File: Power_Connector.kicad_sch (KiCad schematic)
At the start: 4 parts, among them J2 AMASS XT60 Male, J3 AMASS XT60 Male, J7 AMASS XT60 Female

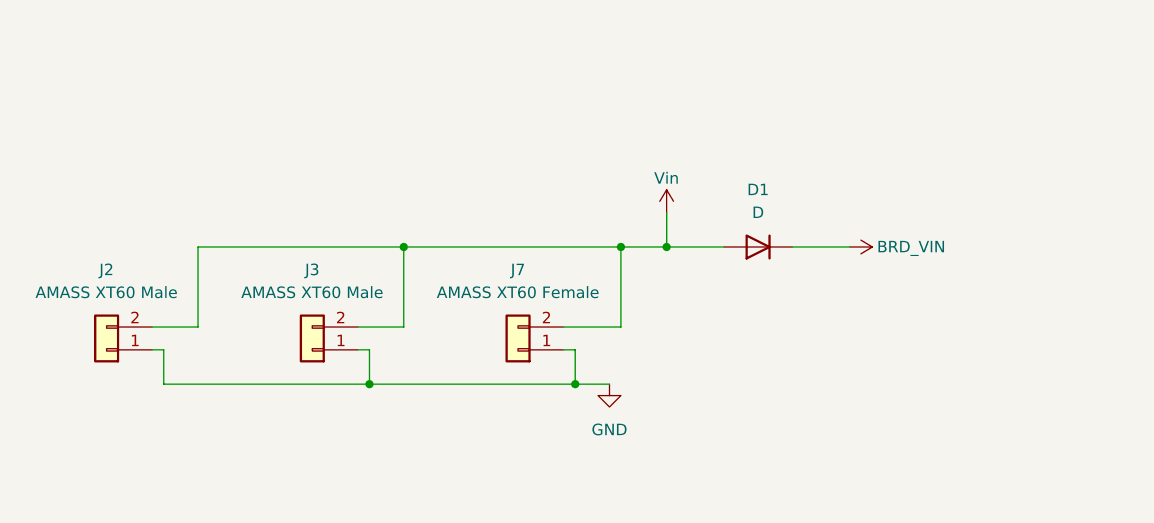
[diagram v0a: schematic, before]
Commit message: finished schematic (without some part numbers)
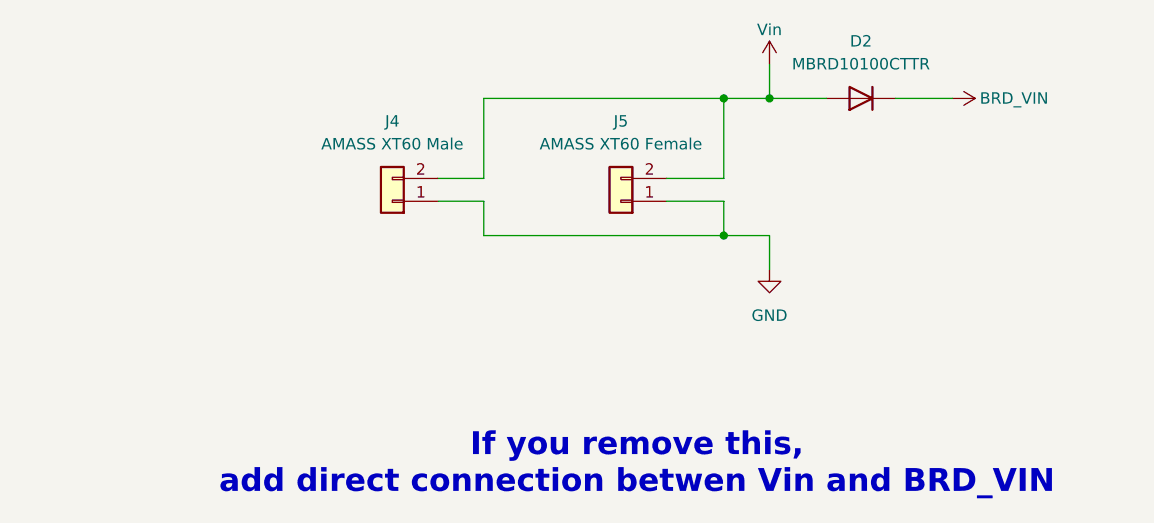
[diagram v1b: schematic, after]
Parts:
- removed D1: D, symbol Device:D
- removed J3: AMASS XT60 Male, XT60:AMASS_XT60PW-M_1x02_P7.20mm_Horizontal, symbol Connector_Generic:Conn_01x02
- added D2: MBRD10100CTTR, symbol Device:D
- renumbered J2 to J4, J7 to J5
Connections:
- net BRD_VIN: now also D2.1 (K)
- net Vin: now also D2.2 (A)
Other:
- note added: "If you remove this, add direct connection betwen Vin and BRD_VIN"
- moved on the sheet: J4, J5

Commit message: initial component placement
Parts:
- D2: footprint (none) -> Package_TO_SOT_SMD:TO-252-2
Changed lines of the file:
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@@
 			)
 		)
-		(property "Footprint" ""
+		(property "Footprint" "Package_TO_SOT_SMD:TO-252-2"
 			(at 167.64 86.36 0)
 			(effects

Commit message: revision
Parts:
- removed D2: MBRD10100CTTR, Package_TO_SOT_SMD:TO-252-2, symbol Device:D
- added D4: MBRD10100CTTR, SMC_MBRD10100CTTR:TO-252-3_L6.5-W5.8-P4.58-TL, symbol SMC_MBRD10100CTTR:MBRD10100CTTR
- J4, J5: now left out of the parts list
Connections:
- net BRD_VIN: now also D4.2 (K)
- net Vin: now also D4.1, D4.3
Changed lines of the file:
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@@
+	)
+	(junction
+		(at 161.29 86.36)
+		(diameter 0)
+		(color 0 0 0 0)
 	)
 	(junction
@@
 	(wire
 		(pts
+			(xy 161.29 86.36) (xy 163.83 86.36)
+		)
+		(stroke
+			(width 0)
+			(type default)
+		)
+	)
+	(wire
+		(pts
 			(xy 152.4 86.36) (xy 157.48 86.36)
 		)
@@
 	(wire
 		(pts
-			(xy 157.48 86.36) (xy 163.83 86.36)
+			(xy 157.48 86.36) (xy 161.29 86.36)
+		)
+		(stroke
+			(width 0)
+			(type default)
+		)
+	)
+	(wire
+		(pts
+			(xy 161.29 91.44) (xy 161.29 86.36)
+		)
+		(stroke
+			(width 0)
+			(type default)
+		)
+	)
+	(wire
+		(pts
+			(xy 163.83 91.44) (xy 161.29 91.44)
 		)
 		(stroke
@@
 	(wire
 		(pts
-			(xy 171.45 86.36) (xy 177.8 86.36)
+			(xy 179.07 88.9) (xy 185.42 88.9)
 		)
 		(stroke
@@
 		(unit 1)
 		(exclude_from_sim no)
-		(in_bom yes)
+		(in_bom no)
 		(on_board yes)
 		(dnp no)
@@
 	(symbol
 		(lib_id "power:VCC")
-		(at 177.8 86.36 270)
+		(at 185.42 88.9 270)
 		(unit 1)
 		(exclude_from_sim no)
@@
 		(on_board yes)
 		(dnp no)
-		(property "Reference" "#PWR041"
-			(at 173.99 86.36 0)
+		(property "Reference" "#PWR042"
+			(at 181.61 88.9 0)
 			(effects
 				(font
@@
 		)
 		(property "Value" "BRD_VIN"
-			(at 184.658 86.36 90)
+			(at 192.278 88.9 90)
 			(effects
 				(font
@@
 		)
 		(property "Footprint" ""
-			(at 177.8 86.36 0)
+			(at 185.42 88.9 0)
 			(effects
 				(font
@@
 		)
 		(property "Datasheet" ""
-			(at 177.8 86.36 0)
+			(at 185.42 88.9 0)
 			(effects
 				(font
@@
 		)
 		(property "Description" "Power symbol creates a global label with name \"VCC\""
-			(at 177.8 86.36 0)
+			(at 185.42 88.9 0)
 			(effects
 				(font
@@
 			(project "MMS2_hat_template_small"
 				(path "/6596548a-44e0-46d8-8624-fd71cf4a3e17/f11c3b61-ae6a-4858-9d37-bbf426f44fb0"
-					(reference "#PWR041")
+					(reference "#PWR042")
 					(unit 1)
 				)
@@
 		(unit 1)
 		(exclude_from_sim no)
-		(in_bom yes)
+		(in_bom no)
 		(on_board yes)
 		(dnp no)
@@
 		(on_board yes)
 		(dnp no)
-		(property "Reference" "#PWR039"
+		(property "Reference" "#PWR040"
 			(at 157.48 86.36 0)
 			(effects
@@
 			(project "MMS2_hat_template_small"
 				(path "/6596548a-44e0-46d8-8624-fd71cf4a3e17/f11c3b61-ae6a-4858-9d37-bbf426f44fb0"
-					(reference "#PWR039")
+					(reference "#PWR040")
 					(unit 1)
 				)
@@
 	)
 	(symbol
-		(lib_id "Device:D")
-		(at 167.64 86.36 180)
+		(lib_id "SMC_MBRD10100CTTR:MBRD10100CTTR")
+		(at 171.45 88.9 0)
 		(unit 1)
 		(exclude_from_sim no)
@@
 		(dnp no)
 		(fields_autoplaced yes)
-		(property "Reference" "D2"
-			(at 167.64 80.01 0)
-			(effects
-				(font
-					(size 1.27 1.27)
-				)
+		(property "Reference" "D4"
+			(at 172.7201 93.98 90)
+			(effects
+				(font
+					(size 1.27 1.27)
+				)
+				(justify right)
 			)
 		)
 		(property "Value" "MBRD10100CTTR"
-			(at 167.64 82.55 0)
-			(effects
-				(font
-					(size 1.27 1.27)
-				)
-			)
-		)
-		(property "Footprint" "Package_TO_SOT_SMD:TO-252-2"
-			(at 167.64 86.36 0)
-			(effects
-				(font
-					(size 1.27 1.27)
-				)
-				(hide yes)
-			)
-		)
-		(property "Datasheet" "~"
-			(at 167.64 86.36 0)
-			(effects
-				(font
-					(size 1.27 1.27)
-				)
-				(hide yes)
-			)
-		)
-		(property "Description" "Diode"
-			(at 167.64 86.36 0)
-			(effects
-				(font
-					(size 1.27 1.27)
-				)
-				(hide yes)
-			)
-		)
-		(property "Sim.Device" "D"
-			(at 167.64 86.36 0)
-			(effects
-				(font
-					(size 1.27 1.27)
-				)
-				(hide yes)
-			)
-		)
-		(property "Sim.Pins" "1=K 2=A"
-			(at 167.64 86.36 0)
-			(effects
-				(font
-					(size 1.27 1.27)
-				)
-				(hide yes)
-			)
-		)
-		(property "LCSC" "C135494"
-			(at 167.64 86.36 90)
-			(effects
-				(font
-					(size 1.27 1.27)
-				)
-				(hide yes)
-			)
+			(at 170.1801 93.98 90)
+			(effects
+				(font
+					(size 1.27 1.27)
+				)
+				(justify right)
+			)
+		)
+		(property "Footprint" "SMC_MBRD10100CTTR:TO-252-3_L6.5-W5.8-P4.58-TL"
+			(at 171.45 99.06 0)
+			(effects
+				(font
+					(size 1.27 1.27)
+				)
+				(hide yes)
+			)
+		)
+		(property "Datasheet" "https://lcsc.com/product-detail/Schottky-Barrier-Diodes-SBD_MCC_MBRD10100CTTR_MBRD10100CTTR_C135494.html"
+			(at 171.45 101.6 0)
+			(effects
+				(font
+					(size 1.27 1.27)
+				)
+				(hide yes)
+			)
+		)
+		(property "Description" ""
+			(at 171.45 88.9 0)
+			(effects
+				(font
+					(size 1.27 1.27)
+				)
+				(hide yes)
+			)
+		)
+		(property "LCSC Part" "C135494"
+			(at 171.45 104.14 0)
+			(effects
+				(font
+					(size 1.27 1.27)
+				)
+				(hide yes)
+			)
+		)
+		(pin "1"
 		)
 		(pin "2"
 		)
-		(pin "1"
+		(pin "3"
 		)
 		(instances
 			(project "MMS3_hat_stepper_controler"
 				(path "/6596548a-44e0-46d8-8624-fd71cf4a3e17/f11c3b61-ae6a-4858-9d37-bbf426f44fb0"
-					(reference "D2")
+					(reference "D4")
 					(unit 1)
 				)
@@
 		(dnp no)
 		(fields_autoplaced yes)
-		(property "Reference" "#PWR040"
+		(property "Reference" "#PWR041"
 			(at 157.48 111.76 0)
 			(effects
@@
 			(project ""
 				(path "/6596548a-44e0-46d8-8624-fd71cf4a3e17/f11c3b61-ae6a-4858-9d37-bbf426f44fb0"
-					(reference "#PWR040")
+					(reference "#PWR041")
 					(unit 1)
 				)

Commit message: second component placement
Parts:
- renumbered D4 to D2
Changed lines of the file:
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@@
+			)
+		)
+		(property "Sim.Device" ""
+			(at 115.57 97.79 0)
+			(effects
+				(font
+					(size 1.27 1.27)
+				)
+				(hide yes)
 			)
 		)
@@
 		(on_board yes)
 		(dnp no)
-		(property "Reference" "#PWR042"
+		(property "Reference" "#PWR041"
 			(at 181.61 88.9 0)
 			(effects
@@
 			(project "MMS2_hat_template_small"
 				(path "/6596548a-44e0-46d8-8624-fd71cf4a3e17/f11c3b61-ae6a-4858-9d37-bbf426f44fb0"
-					(reference "#PWR042")
+					(reference "#PWR041")
 					(unit 1)
 				)
@@
 			)
 		)
+		(property "Sim.Device" ""
+			(at 140.97 97.79 0)
+			(effects
+				(font
+					(size 1.27 1.27)
+				)
+				(hide yes)
+			)
+		)
 		(pin "1"
 		)
@@
 		(on_board yes)
 		(dnp no)
-		(property "Reference" "#PWR040"
+		(property "Reference" "#PWR039"
 			(at 157.48 86.36 0)
 			(effects
@@
 			(project "MMS2_hat_template_small"
 				(path "/6596548a-44e0-46d8-8624-fd71cf4a3e17/f11c3b61-ae6a-4858-9d37-bbf426f44fb0"
-					(reference "#PWR040")
+					(reference "#PWR039")
 					(unit 1)
 				)
@@
 		(dnp no)
 		(fields_autoplaced yes)
-		(property "Reference" "D4"
+		(property "Reference" "D2"
 			(at 172.7201 93.98 90)
 			(effects
@@
 			)
 		)
+		(property "Sim.Device" ""
+			(at 171.45 88.9 90)
+			(effects
+				(font
+					(size 1.27 1.27)
+				)
+				(hide yes)
+			)
+		)
 		(pin "1"
 		)
@@
 			(project "MMS3_hat_stepper_controler"
 				(path "/6596548a-44e0-46d8-8624-fd71cf4a3e17/f11c3b61-ae6a-4858-9d37-bbf426f44fb0"
-					(reference "D4")
+					(reference "D2")
 					(unit 1)
 				)
@@
 		(dnp no)
 		(fields_autoplaced yes)
-		(property "Reference" "#PWR041"
+		(property "Reference" "#PWR040"
 			(at 157.48 111.76 0)
 			(effects
@@
 			(project ""
 				(path "/6596548a-44e0-46d8-8624-fd71cf4a3e17/f11c3b61-ae6a-4858-9d37-bbf426f44fb0"
-					(reference "#PWR041")
-					(unit 1)
-				)
+					(reference "#PWR040")
+					(unit 1)
+				)

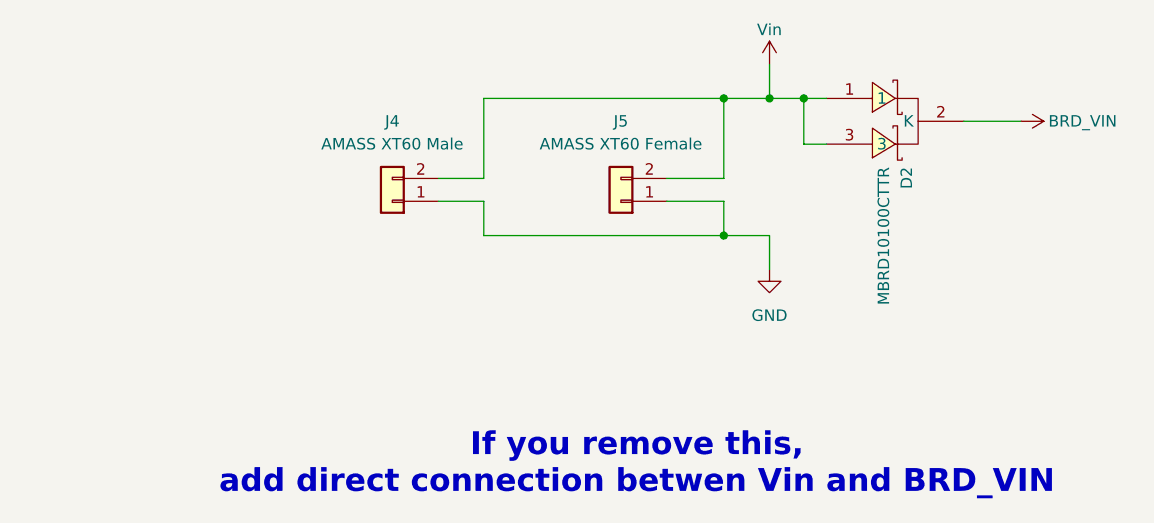
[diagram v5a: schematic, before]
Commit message: added clearance for mounting
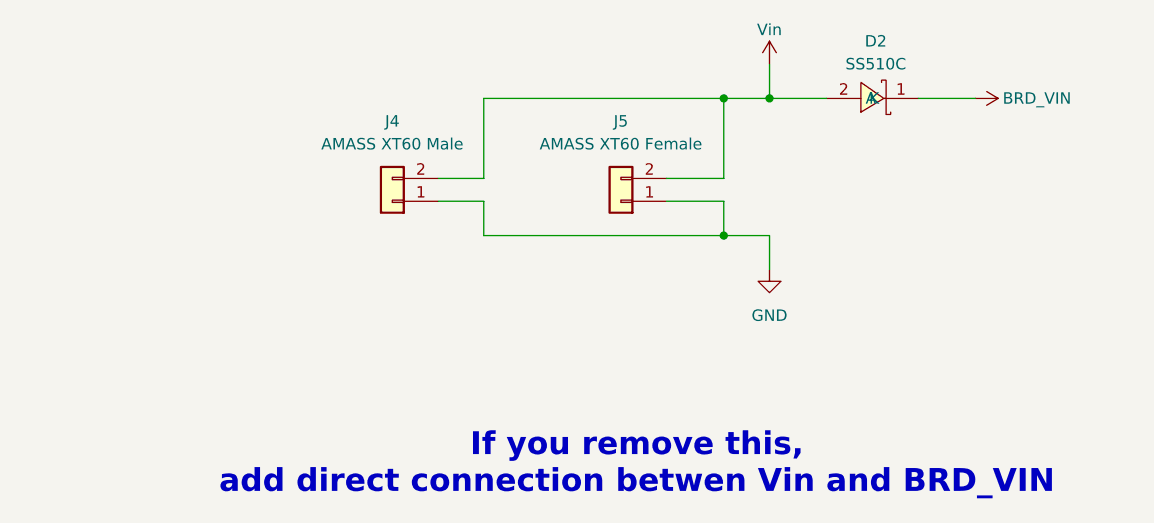
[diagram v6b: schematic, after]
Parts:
- removed D2: MBRD10100CTTR, SMC_MBRD10100CTTR:TO-252-3_L6.5-W5.8-P4.58-TL, symbol SMC_MBRD10100CTTR:MBRD10100CTTR
- added D2: SS510C, SS510C:SMC_L7.1-W6.2-LS8.1-RD, symbol SS510C:SS510C
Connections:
- net BRD_VIN: now also D2.1 (K)
- net Vin: now also D2.2 (A)
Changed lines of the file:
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@@
-	)
-	(junction
-		(at 161.29 86.36)
-		(diameter 0)
-		(color 0 0 0 0)
 	)
 	(junction
@@
 	(wire
 		(pts
-			(xy 161.29 86.36) (xy 163.83 86.36)
-		)
-		(stroke
-			(width 0)
-			(type default)
-		)
-	)
-	(wire
-		(pts
 			(xy 152.4 86.36) (xy 157.48 86.36)
 		)
@@
 	(wire
 		(pts
-			(xy 157.48 86.36) (xy 161.29 86.36)
-		)
-		(stroke
-			(width 0)
-			(type default)
-		)
-	)
-	(wire
-		(pts
-			(xy 161.29 91.44) (xy 161.29 86.36)
-		)
-		(stroke
-			(width 0)
-			(type default)
-		)
-	)
-	(wire
-		(pts
-			(xy 163.83 91.44) (xy 161.29 91.44)
+			(xy 157.48 86.36) (xy 163.83 86.36)
 		)
 		(stroke
@@
 	(wire
 		(pts
-			(xy 179.07 88.9) (xy 185.42 88.9)
+			(xy 173.99 86.36) (xy 180.34 86.36)
 		)
 		(stroke
@@
 	(symbol
 		(lib_id "power:VCC")
-		(at 185.42 88.9 270)
+		(at 180.34 86.36 270)
 		(unit 1)
 		(exclude_from_sim no)
@@
 		(dnp no)
 		(property "Reference" "#PWR041"
-			(at 181.61 88.9 0)
+			(at 176.53 86.36 0)
 			(effects
 				(font
@@
 		)
 		(property "Value" "BRD_VIN"
-			(at 192.278 88.9 90)
+			(at 187.198 86.36 90)
 			(effects
 				(font
@@
 		)
 		(property "Footprint" ""
-			(at 185.42 88.9 0)
+			(at 180.34 86.36 0)
 			(effects
 				(font
@@
 		)
 		(property "Datasheet" ""
-			(at 185.42 88.9 0)
+			(at 180.34 86.36 0)
 			(effects
 				(font
@@
 		)
 		(property "Description" "Power symbol creates a global label with name \"VCC\""
-			(at 185.42 88.9 0)
+			(at 180.34 86.36 0)
 			(effects
 				(font
@@
 	)
 	(symbol
-		(lib_id "SMC_MBRD10100CTTR:MBRD10100CTTR")
-		(at 171.45 88.9 0)
+		(lib_id "SS510C:SS510C")
+		(at 168.91 86.36 180)
 		(unit 1)
 		(exclude_from_sim no)
@@
 		(fields_autoplaced yes)
 		(property "Reference" "D2"
-			(at 172.7201 93.98 90)
-			(effects
-				(font
-					(size 1.27 1.27)
-				)
-				(justify right)
-			)
-		)
-		(property "Value" "MBRD10100CTTR"
-			(at 170.1801 93.98 90)
-			(effects
-				(font
-					(size 1.27 1.27)
-				)
-				(justify right)
-			)
-		)
-		(property "Footprint" "SMC_MBRD10100CTTR:TO-252-3_L6.5-W5.8-P4.58-TL"
-			(at 171.45 99.06 0)
-			(effects
-				(font
-					(size 1.27 1.27)
-				)
-				(hide yes)
-			)
-		)
-		(property "Datasheet" "https://lcsc.com/product-detail/Schottky-Barrier-Diodes-SBD_MCC_MBRD10100CTTR_MBRD10100CTTR_C135494.html"
-			(at 171.45 101.6 0)
+			(at 169.29 80.01 0)
+			(effects
+				(font
+					(size 1.27 1.27)
+				)
+			)
+		)
+		(property "Value" "SS510C"
+			(at 169.29 82.55 0)
+			(effects
+				(font
+					(size 1.27 1.27)
+				)
+			)
+		)
+		(property "Footprint" "SS510C:SMC_L7.1-W6.2-LS8.1-RD"
+			(at 168.91 78.74 0)
+			(effects
+				(font
+					(size 1.27 1.27)
+				)
+				(hide yes)
+			)
+		)
+		(property "Datasheet" "https://lcsc.com/product-detail/Schottky-Barrier-Diodes-SBD_SS510C_C123944.html"
+			(at 168.91 76.2 0)
 			(effects
 				(font
@@
 		)
 		(property "Description" ""
-			(at 171.45 88.9 0)
-			(effects
-				(font
-					(size 1.27 1.27)
-				)
-				(hide yes)
-			)
-		)
-		(property "LCSC Part" "C135494"
-			(at 171.45 104.14 0)
-			(effects
-				(font
-					(size 1.27 1.27)
-				)
-				(hide yes)
-			)
-		)
-		(property "Sim.Device" ""
-			(at 171.45 88.9 90)
-			(effects
-				(font
-					(size 1.27 1.27)
-				)
-				(hide yes)
-			)
+			(at 168.91 86.36 0)
+			(effects
+				(font
+					(size 1.27 1.27)
+				)
+				(hide yes)
+			)
+		)
+		(property "Manufacturer" "晶导微电子"
+			(at 168.91 73.66 0)
+			(effects
+				(font
+					(size 1.27 1.27)
+				)
+				(hide yes)
+			)
+		)
+		(property "MPN" "SS510C"
+			(at 168.91 71.12 0)
+			(effects
+				(font
+					(size 1.27 1.27)
+				)
+				(hide yes)
+			)
+		)
+		(property "LCSC Part" "C123944"
+			(at 168.91 68.58 0)
+			(effects
+				(font
+					(size 1.27 1.27)
+				)
+				(hide yes)
+			)
+		)
+		(pin "2"
 		)
 		(pin "1"
 		)
-		(pin "2"
-		)
-		(pin "3"
-		)
 		(instances
